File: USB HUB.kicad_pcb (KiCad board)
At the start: 2 copper layers, 30 x 91.8 mm, 15 parts, among them J1 USB3_A, J2 USB3_A, J3 USB3_A, J4 USB3_A, J5 Conn_01x09_Socket, U1 FE1.1s, Y1 Crystal_GND24

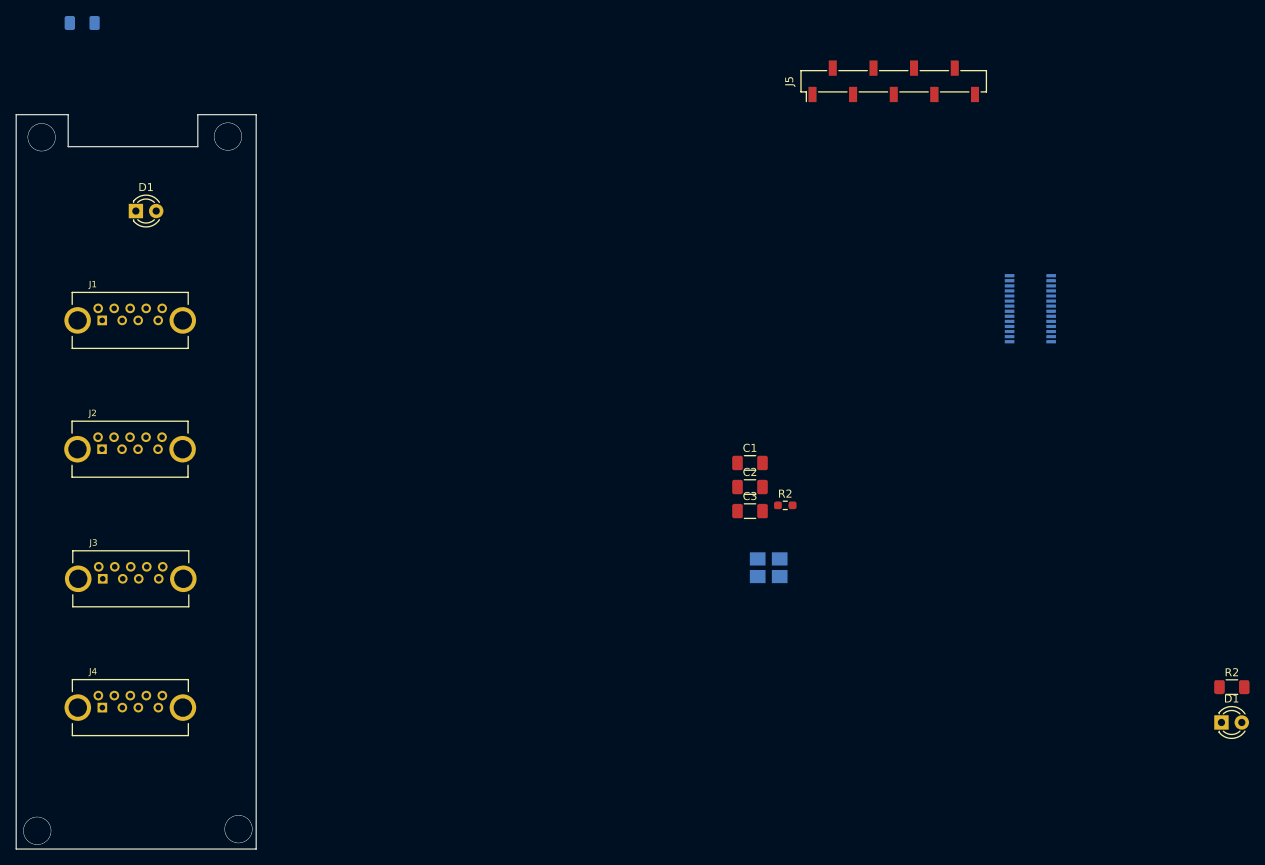
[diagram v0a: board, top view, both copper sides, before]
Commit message: changed foot print for connector and foot prints for capacitors to smaller size, placed components in perfect positions
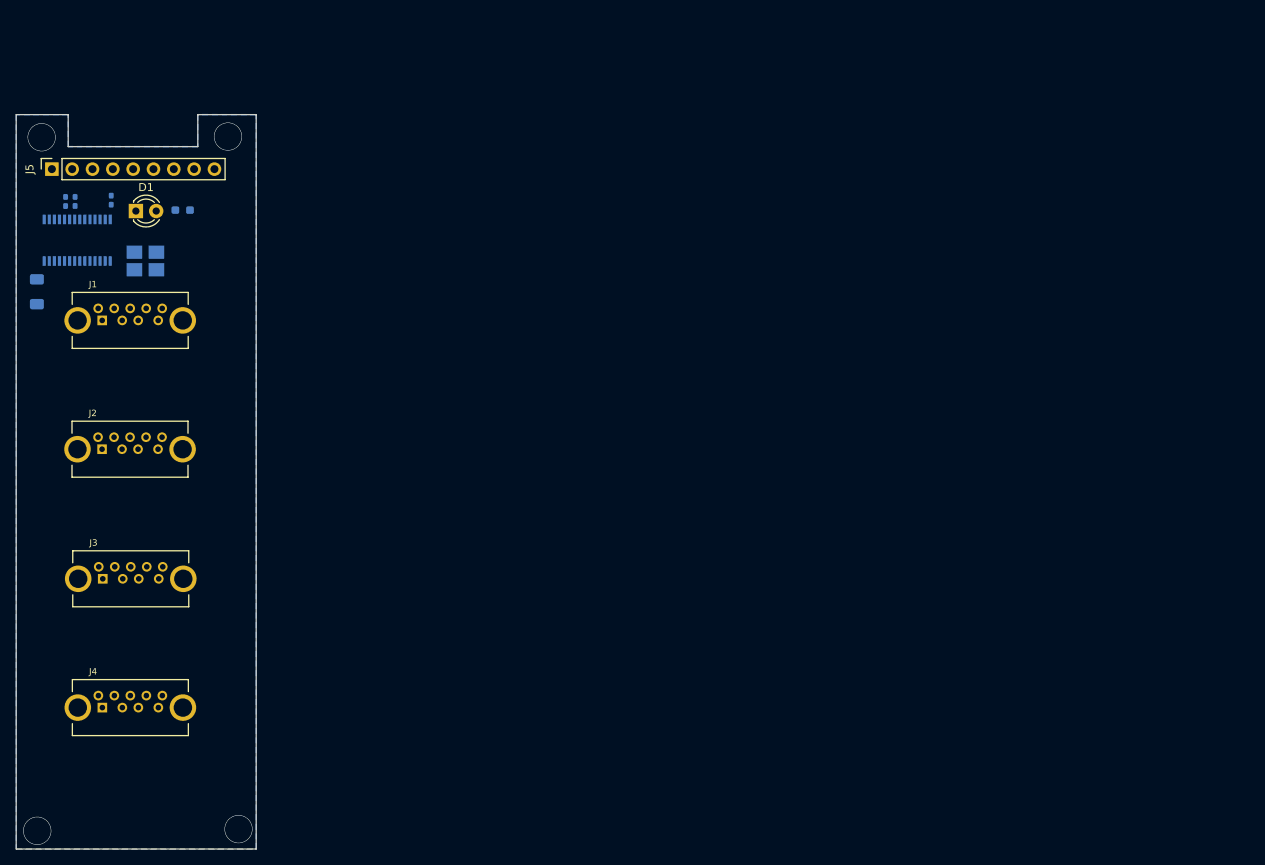
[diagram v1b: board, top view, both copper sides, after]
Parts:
- removed the D1 at (269.0, 113.5)
- removed the R2 at (270.3, 109.1)
- C1, C2, C3: footprint Capacitor_SMD:C_1206_3216Metric_Pad1.33x1.80mm_HandSolder -> Capacitor_SMD:C_0402_1005Metric_Pad0.74x0.62mm_HandSolder; moved to B.Cu
- J5: footprint Connector_PinSocket_2.54mm:PinSocket_1x09_P2.54mm_Vertical_SMD_Pin1Left -> Connector_PinSocket_2.54mm:PinSocket_1x09_P2.54mm_Vertical
- R2: moved to B.Cu
- moved U1 119.4 mm to (125.9, 53.2), turned to 90 degrees
- moved J5 105.8 mm to (122.8, 44.3)
- moved C2 91.6 mm to (125.7, 48.4), turned to 90 degrees
- moved C1 91.6 mm to (124.5, 48.4), turned to 90 degrees
- moved C3 88.8 mm to (130.2, 48.2), turned to 90 degrees
- moved Y1 86.8 mm to (134.4, 55.8)
- moved R2 83.9 mm to (139.1, 49.5)
- moved R1 34.1 mm to (120.9, 59.7), turned to 90 degrees
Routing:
- added copper zone on B.Cu, net GND

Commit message: Test
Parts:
- moved Y1 5.47 mm to (139.9, 56.1)
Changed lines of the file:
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@@
 	(footprint "Oscillator:Oscillator_SMD_Abracon_ASE-4Pin_3.2x2.5mm_HandSoldering"
 		(layer "B.Cu")
-		(at 134.45 55.81 180)
+		(at 139.915 56.11 180)
 		(descr "Miniature Crystal Clock Oscillator Abracon ASE series, http://www.abracon.com/Oscillators/ASEseries.pdf, hand-soldering, 3.2x2.5mm^2 package")
 		(tags "SMD SMT crystal oscillator hand-soldering")
